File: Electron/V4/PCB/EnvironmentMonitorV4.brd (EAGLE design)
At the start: 94 x 31.8 mm, 28 parts, among them U3 ELECTRONDUALNAMED, U5 CCS811, U6 BME280, U7 ALS-PT19, U8 ALS-PT19

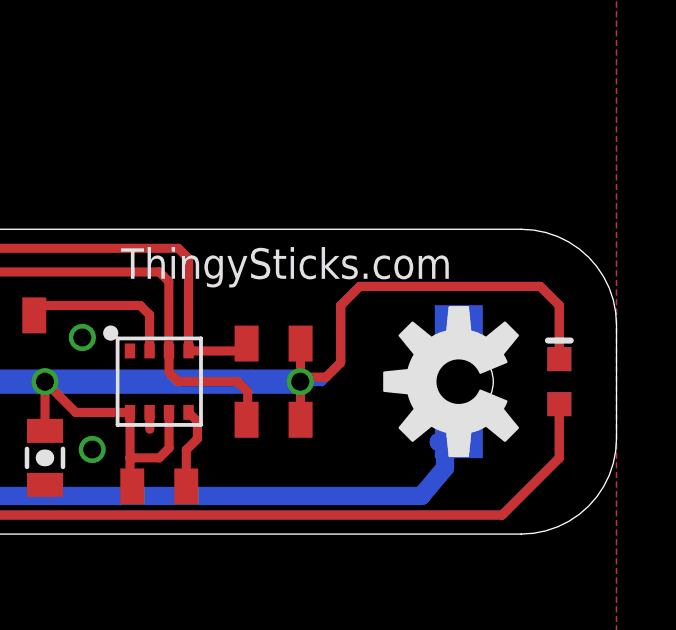
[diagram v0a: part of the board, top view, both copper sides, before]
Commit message: Minor routing updates to give more space. Ran IDF export (hence extra 113 layer)
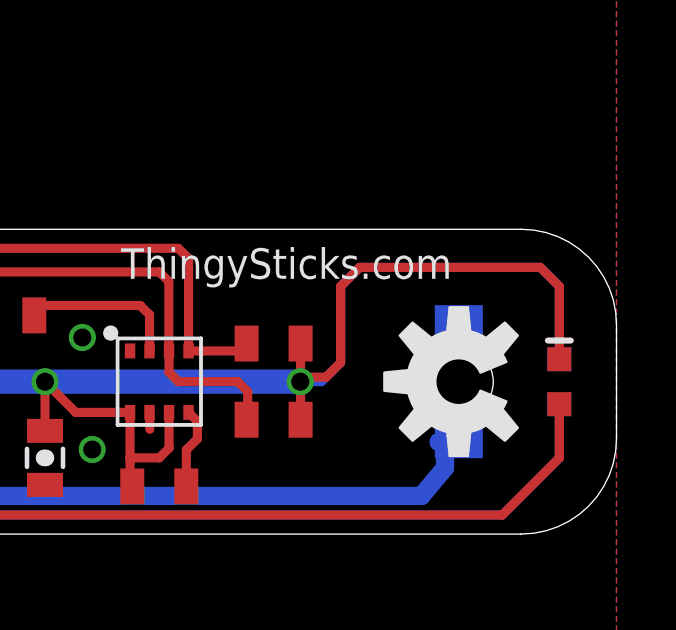
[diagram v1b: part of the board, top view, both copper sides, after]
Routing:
- net 3.3V: track 157.6 -> 160.1 mm
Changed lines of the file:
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@@
 <setting verticaltext="up"/>
 </settings>
-<grid distance="0.025" unitdist="inch" unit="inch" style="lines" multiple="1" display="yes" altdistance="0.006" altunitdist="inch" altunit="inch"/>
+<grid distance="0.1" unitdist="mm" unit="mm" style="lines" multiple="1" display="yes" altdistance="0.006" altunitdist="inch" altunit="inch"/>
 <layers>
 <layer number="1" name="Top" color="4" fill="1" visible="yes" active="yes"/>
@@
 <layer number="23" name="tOrigins" color="15" fill="1" visible="yes" active="yes"/>
 <layer number="24" name="bOrigins" color="15" fill="1" visible="yes" active="yes"/>
-<layer number="25" name="tNames" color="7" fill="1" visible="no" active="yes"/>
+<layer number="25" name="tNames" color="7" fill="1" visible="yes" active="yes"/>
 <layer number="26" name="bNames" color="7" fill="1" visible="yes" active="yes"/>
-<layer number="27" name="tValues" color="7" fill="1" visible="no" active="yes"/>
-<layer number="28" name="bValues" color="7" fill="1" visible="no" active="yes"/>
+<layer number="27" name="tValues" color="7" fill="1" visible="yes" active="yes"/>
+<layer number="28" name="bValues" color="7" fill="1" visible="yes" active="yes"/>
 <layer number="29" name="tStop" color="7" fill="3" visible="yes" active="yes"/>
 <layer number="30" name="bStop" color="7" fill="6" visible="yes" active="yes"/>
@@
 <layer number="111" name="LPC17xx" color="7" fill="1" visible="yes" active="yes"/>
 <layer number="112" name="tSilk" color="7" fill="1" visible="yes" active="yes"/>
-<layer number="113" name="IDFDebug" color="4" fill="1" visible="yes" active="yes"/>
+<layer number="113" name="IDFDebug" color="4" fill="1" visible="no" active="yes"/>
 <layer number="114" name="Badge_Outline" color="7" fill="1" visible="yes" active="yes"/>
 <layer number="115" name="ReferenceISLANDS" color="7" fill="1" visible="yes" active="yes"/>
@@
 <text x="77.47" y="19.304" size="1.016" layer="25" font="vector">ThingySticks.com</text>
 <text x="87.0966" y="19.1262" size="1.27" layer="26" font="vector" rot="MR0">ThingySticks.com</text>
+<circle x="-8.8" y="2.475" radius="1.999996875" width="0.4064" layer="113"/>
+<wire x1="-0.4" y1="3.075" x2="0" y2="28.575025" width="0.254" layer="113"/>
+<wire x1="0" y1="28.575025" x2="0.20116875" y2="29.468115625" width="0.254" layer="113"/>
+<wire x1="0.20116875" y1="29.468115625" x2="0.62664375" y2="30.27873125" width="0.254" layer="113"/>
+<wire x1="0.62664375" y1="30.27873125" x2="1.24744375" y2="30.951603125" width="0.254" layer="113"/>
+<wire x1="1.24744375" y1="30.951603125" x2="2.02120625" y2="31.44085625" width="0.254" layer="113"/>
+<wire x1="2.02120625" y1="31.44085625" x2="2.89526875" y2="31.713196875" width="0.254" layer="113"/>
+<wire x1="2.89526875" y1="31.713196875" x2="3.81" y2="31.750025" width="0.254" layer="113"/>
+<wire x1="3.81" y1="31.750025" x2="52.070025" y2="31.750025" width="0.254" layer="113"/>
+<wire x1="52.070025" y1="31.750025" x2="52.798778125" y2="31.570471875" width="0.254" layer="113"/>
+<wire x1="52.798778125" y1="31.570471875" x2="53.45623125" y2="31.208421875" width="0.254" layer="113"/>
+<wire x1="53.45623125" y1="31.208421875" x2="53.99758125" y2="30.688559375" width="0.254" layer="113"/>
+<wire x1="53.99758125" y1="30.688559375" x2="54.385946875" y2="30.04629375" width="0.254" layer="113"/>
+<wire x1="54.385946875" y1="30.04629375" x2="54.5948375" y2="29.32541875" width="0.254" layer="113"/>
+<wire x1="54.5948375" y1="29.32541875" x2="54.610025" y2="28.575025" width="0.254" layer="113"/>
+<wire x1="54.610025" y1="28.575025" x2="54.610025" y2="23.495" width="0.254" layer="113"/>
+<wire x1="54.610025" y1="23.495" x2="54.6965875" y2="22.837621875" width="0.254" layer="113"/>
+<wire x1="54.6965875" y1="22.837621875" x2="54.950334375" y2="22.225" width="0.254" layer="113"/>
+<wire x1="54.950334375" y1="22.225" x2="55.353990625" y2="21.698965625" width="0.254" layer="113"/>
+<wire x1="55.353990625" y1="21.698965625" x2="55.880025" y2="21.295309375" width="0.254" layer="113"/>
+<wire x1="55.880025" y1="21.295309375" x2="56.492621875" y2="21.0415625" width="0.254" layer="113"/>
+<wire x1="56.492621875" y1="21.0415625" x2="57.150025" y2="20.955" width="0.254" layer="113"/>
+<wire x1="57.150025" y1="20.955" x2="90.80505" y2="20.955" width="0.254" layer="113"/>
+<wire x1="90.80505" y1="20.955" x2="91.626790625" y2="20.846821875" width="0.254" layer="113"/>
+<wire x1="91.626790625" y1="20.846821875" x2="92.39255" y2="20.529653125" width="0.254" layer="113"/>
+<wire x1="92.39255" y1="20.529653125" x2="93.05010625" y2="20.02508125" width="0.254" layer="113"/>
+<wire x1="93.05010625" y1="20.02508125" x2="93.554678125" y2="19.3675" width="0.254" layer="113"/>
+<wire x1="93.554678125" y1="19.3675" x2="93.871871875" y2="18.601765625" width="0.254" layer="113"/>
+<wire x1="93.871871875" y1="18.601765625" x2="93.98005" y2="17.78" width="0.254" layer="113"/>
+<wire x1="93.98005" y1="17.78" x2="93.98005" y2="13.97" width="0.254" layer="113"/>
+<wire x1="93.98005" y1="13.97" x2="93.871871875" y2="13.148259375" width="0.254" layer="113"/>
+<wire x1="93.871871875" y1="13.148259375" x2="93.554678125" y2="12.3825" width="0.254" layer="113"/>
+<wire x1="93.554678125" y1="12.3825" x2="93.05010625" y2="11.72494375" width="0.254" layer="113"/>
+<wire x1="93.05010625" y1="11.72494375" x2="92.39255" y2="11.220375" width="0.254" layer="113"/>
+<wire x1="92.39255" y1="11.220375" x2="91.626790625" y2="10.903178125" width="0.254" layer="113"/>
+<wire x1="91.626790625" y1="10.903178125" x2="90.80505" y2="10.795" width="0.254" layer="113"/>
+<wire x1="90.80505" y1="10.795" x2="57.150025" y2="10.795" width="0.254" layer="113"/>
+<wire x1="57.150025" y1="10.795" x2="56.492621875" y2="10.7084625" width="0.254" layer="113"/>
+<wire x1="56.492621875" y1="10.7084625" x2="55.880025" y2="10.454715625" width="0.254" layer="113"/>
+<wire x1="55.880025" y1="10.454715625" x2="55.353990625" y2="10.051059375" width="0.254" layer="113"/>
+<wire x1="55.353990625" y1="10.051059375" x2="54.950334375" y2="9.525" width="0.254" layer="113"/>
+<wire x1="54.950334375" y1="9.525" x2="54.6965875" y2="8.912403125" width="0.254" layer="113"/>
+<wire x1="54.6965875" y1="8.912403125" x2="54.610025" y2="8.255" width="0.254" layer="113"/>
+<wire x1="54.610025" y1="8.255" x2="54.610025" y2="3.175" width="0.254" layer="113"/>
+<wire x1="54.610025" y1="3.175" x2="54.5948375" y2="2.42460625" width="0.254" layer="113"/>
+<wire x1="54.5948375" y1="2.42460625" x2="54.385946875" y2="1.70370625" width="0.254" layer="113"/>
+<wire x1="54.385946875" y1="1.70370625" x2="53.99758125" y2="1.061440625" width="0.254" layer="113"/>
+<wire x1="53.99758125" y1="1.061440625" x2="53.45623125" y2="0.541578125" width="0.254" layer="113"/>
+<wire x1="53.45623125" y1="0.541578125" x2="52.798778125" y2="0.179553125" width="0.254" layer="113"/>
+<wire x1="52.798778125" y1="0.179553125" x2="52.070025" y2="0" width="0.254" layer="113"/>
+<wire x1="52.070025" y1="0" x2="3.81" y2="0" width="0.254" layer="113"/>
+<wire x1="3.81" y1="0" x2="2.89526875" y2="0.03683125" width="0.254" layer="113"/>
+<wire x1="2.89526875" y1="0.03683125" x2="2.02120625" y2="0.30914375" width="0.254" layer="113"/>
+<wire x1="2.02120625" y1="0.30914375" x2="1.24744375" y2="0.798425" width="0.254" layer="113"/>
+<wire x1="1.24744375" y1="0.798425" x2="0.62664375" y2="1.47129375" width="0.254" layer="113"/>
+<wire x1="0.62664375" y1="1.47129375" x2="0.30116875" y2="2.181884375" width="0.254" layer="113"/>
+<wire x1="0.30116875" y1="2.181884375" x2="-0.4" y2="3.075" width="0.254" layer="113"/>
 </plain>
 <attributes>
@@
 <wire x1="79.065" y1="13.66" x2="78.74" y2="13.335" width="0.3048" layer="1"/>
 <wire x1="78.74" y1="13.335" x2="77.765" y2="13.335" width="0.3048" layer="1"/>
-<wire x1="92.075" y1="18.415" x2="91.44" y2="19.05" width="0.3048" layer="16"/>
-<wire x1="91.44" y1="19.05" x2="85.4202" y2="19.05" width="0.3048" layer="16"/>
-<wire x1="85.4202" y1="19.05" x2="84.7852" y2="18.415" width="0.3048" layer="16"/>
-<wire x1="84.7852" y1="18.415" x2="84.7852" y2="16.51" width="0.3048" layer="16"/>
+<wire x1="92.075" y1="19.05" x2="91.44" y2="19.685" width="0.3048" layer="16"/>
+<wire x1="91.44" y1="19.685" x2="85.4202" y2="19.685" width="0.3048" layer="16"/>
+<wire x1="85.4202" y1="19.685" x2="84.7852" y2="19.05" width="0.3048" layer="16"/>
+<wire x1="84.7852" y1="19.05" x2="84.7852" y2="16.51" width="0.3048" layer="16"/>
 <wire x1="84.7852" y1="16.51" x2="84.1502" y2="15.875" width="0.3048" layer="16"/>
 <wire x1="84.1502" y1="15.875" x2="83.439" y2="15.875" width="0.3048" layer="16"/>
-<wire x1="92.075" y1="16.625" x2="92.075" y2="18.415" width="0.3048" layer="16"/>
+<wire x1="92.075" y1="16.625" x2="92.075" y2="19.05" width="0.3048" layer="16"/>
 <wire x1="60.96" y1="14.605" x2="60.9346" y2="14.605" width="0.3048" layer="1"/>
 <wire x1="60.9346" y1="14.605" x2="60.8076" y2="14.478" width="0.3048" layer="1"/>
 <wire x1="3.81" y1="24.765" x2="3.81" y2="27.305" width="0.8128" layer="1"/>
-<wire x1="92.075" y1="16.625" x2="92.075" y2="18.415" width="0.3048" layer="1"/>
-<wire x1="92.075" y1="18.415" x2="91.44" y2="19.05" width="0.3048" layer="1"/>
-<wire x1="91.44" y1="19.05" x2="85.4202" y2="19.05" width="0.3048" layer="1"/>
-<wire x1="85.4202" y1="19.05" x2="84.7852" y2="18.415" width="0.3048" layer="1"/>
-<wire x1="84.7852" y1="18.415" x2="84.7852" y2="16.51" width="0.3048" layer="1"/>
+<wire x1="92.075" y1="16.625" x2="92.075" y2="19.05" width="0.3048" layer="1"/>
+<wire x1="92.075" y1="19.05" x2="91.44" y2="19.685" width="0.3048" layer="1"/>
+<wire x1="91.44" y1="19.685" x2="85.4202" y2="19.685" width="0.3048" layer="1"/>
+<wire x1="85.4202" y1="19.685" x2="84.7852" y2="19.05" width="0.3048" layer="1"/>
+<wire x1="84.7852" y1="19.05" x2="84.7852" y2="16.51" width="0.3048" layer="1"/>
 <wire x1="84.7852" y1="16.51" x2="84.3026" y2="16.0274" width="0.3048" layer="1"/>
 <wire x1="84.3026" y1="16.0274" x2="83.5914" y2="16.0274" width="0.3048" layer="1"/>

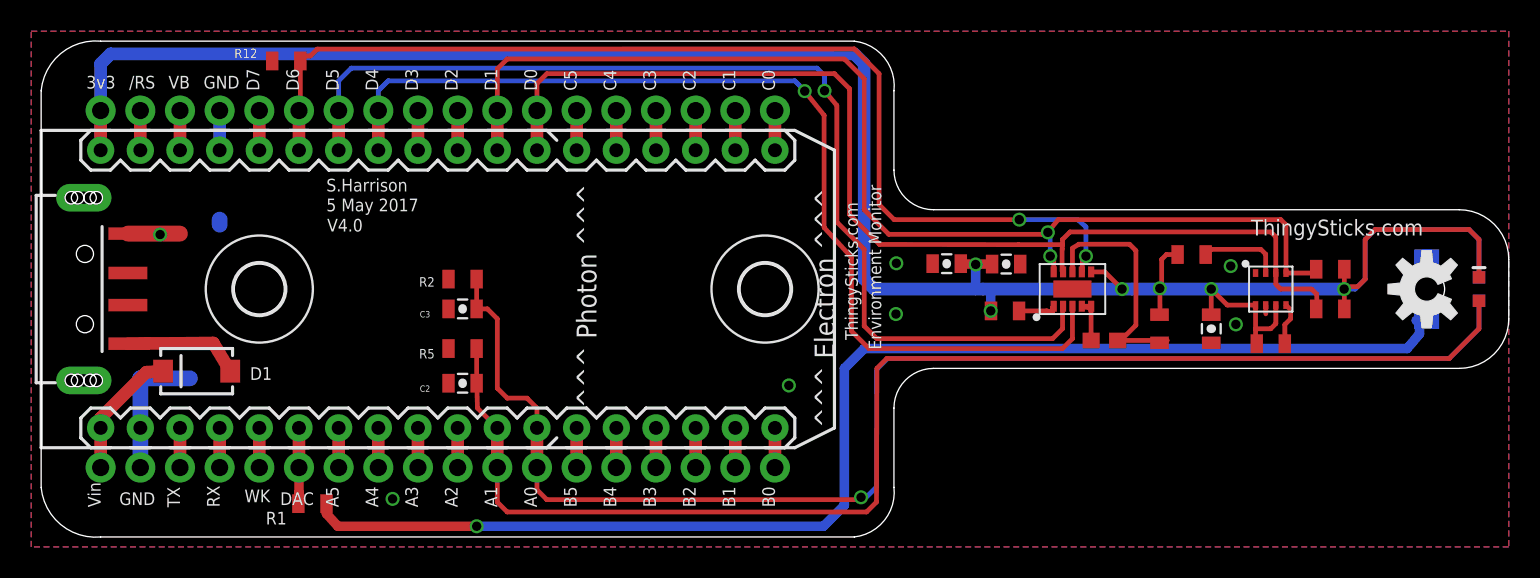
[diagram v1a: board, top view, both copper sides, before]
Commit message: Update V4.0 PCB to use TEMT6000 rather than the diode which requires amplification, and removed rear sensor.
Ordered from DirtyPCBs.
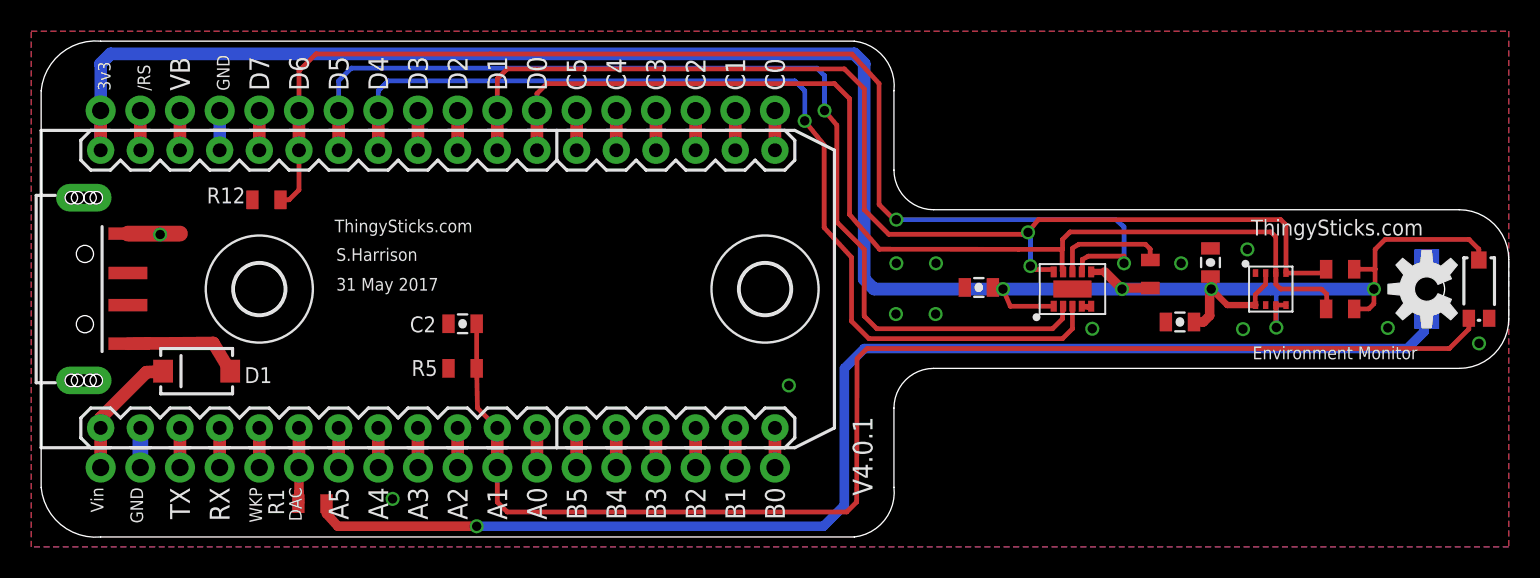
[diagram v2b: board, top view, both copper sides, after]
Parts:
- removed C3: 1.0uF, SparkFun-Capacitors:0805-CAP
- removed R10: 10k, CCS811_Breakout_Temp:0603
- removed R2: (no value), SparkFun-Resistors:0805
- removed R6, R9: 100k, SparkFun-Resistors:0805
- removed R8: 4k7, SparkFun-Resistors:0805
- removed U7, U8: ALS-PT19, SparkFun-Sensors:ALS-PT19
- added U1: LIGHTSENSORTEMT6000, SparkFun-Sensors:TEMT6000-SEN
- C1: value 1.0uF -> 0.1uF
- C2: value 1.0uF -> DNP
- R1: value (none) -> 1k5
- R3, R4: value (none) -> 4k7
- R5: value (none) -> 10k
- moved C4 13.1 mm to (74.9, 17.6), turned to 270 degrees
- moved R12 8.98 mm to (14.4, 21.6)
- moved C2 3.81 mm to (27.0, 13.7)
- moved R11 3.55 mm to (71.0, 16.8), turned to 90 degrees
- moved C1 2.56 mm to (60.0, 16.0)
- moved C5 2.05 mm to (72.9, 13.8), turned to 0 degrees
- moved R5 1.27 mm to (27.0, 10.8)
- moved R3 0.64 mm to (83.2, 14.6)
- moved R4 0.64 mm to (83.2, 17.1)
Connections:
- removed net BME280_CS: R8.2, U6.2
- removed net N$3: R6.2, U6.5
- removed net N$9: R9.2, U5.1
- net 3.3V: now also U1.COLLECTOR, U5.1, U6.2, U6.5; no longer R6.1, R8.1, R9.1, U7.C, U8.C
- net AUX: no longer R10.2
- net GND: no longer C3.1, R2.1
- net LIGHTLEVEL_FRONT: now also U1.EMITTER; no longer U7.E
- net LIGHTLEVEL_REAR: no longer C3.2, R2.2, U8.E
- net NTC_SENSE: no longer R10.1
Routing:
- net LIGHTLEVEL_REAR: track 88.2 -> 3.17 mm, vias 1 -> 0
- net 3.3V: track 160.1 -> 141.3 mm, vias 6 -> 5
- net WAKE: track 69.0 -> 78.0 mm
- net AUX: track 15.8 -> 7.40 mm
- net GND: track 15.7 -> 8.43 mm, vias 7 -> 13
- net BME280_CS: track 5.31 -> 0.00 mm
- net N$3: track 2.74 -> 0.00 mm
- net N$9: track 2.56 -> 0.00 mm
- net NTC_SENSE: track 3.26 -> 1.21 mm
- net RESET: track 67.9 -> 66.6 mm
- net INT: track 65.1 -> 63.8 mm
- net SCL: track 74.0 -> 74.6 mm
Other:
- board text added: "31 May 2017"
- board text added: "Github.com/ThingySticks/EnvironmentMonitor"
- board text added: "V4.0.1"
- board text removed: "5 May 2017"
- board text removed: "V4.0"
- board text removed: "^^^ Electron ^^^"
- board text removed: "^^^ Photon ^^^"
